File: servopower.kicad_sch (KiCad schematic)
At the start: 53 parts, among them IC1 SIC437DED-T1-GE3, U10 MP28167GQ-A-Z, U9 SC4215

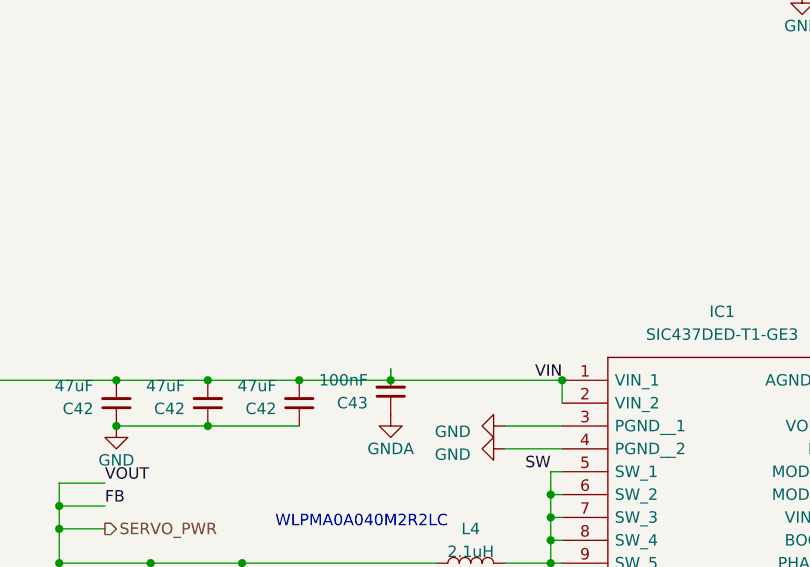
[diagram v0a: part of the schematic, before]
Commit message: latest channges
dont understand why making more copper is good for thermal
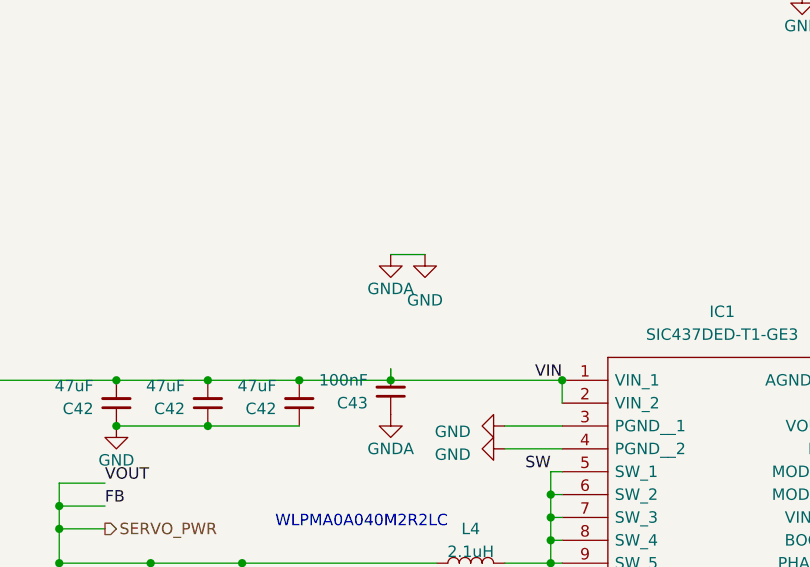
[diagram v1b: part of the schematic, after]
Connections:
- net GNDA is gone; now on net GND: C43.1, C44.2, IC1.16 (AGND_1), IC1.25 (AGND_2), R19.2, R22.2
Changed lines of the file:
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@@
+    (stroke (width 0) (type default))
+  )
+  (wire (pts (xy 186.69 97.79) (xy 190.5 97.79))
     (stroke (width 0) (type default))
   )
@@
     )
   )
+  (symbol (lib_name "GNDA_1") (lib_id "power:GNDA") (at 186.69 97.79 0) (unit 1)
+    (in_bom yes) (on_board yes) (dnp no) (fields_autoplaced)
+    (property "Reference" "#PWR0103" (at 186.69 104.14 0)
+      (effects (font (size 1.27 1.27)) hide)
+    )
+    (property "Value" "GNDA" (at 186.69 101.6 0)
+      (effects (font (size 1.27 1.27)))
+    )
+    (property "Footprint" "" (at 186.69 97.79 0)
+      (effects (font (size 1.27 1.27)) hide)
+    )
+    (property "Datasheet" "" (at 186.69 97.79 0)
+      (effects (font (size 1.27 1.27)) hide)
+    )
+    (pin "1")
+    (instances
+      (project "Canardboard"
+        (path "/7db990e4-92e1-4f99-b4d2-435bbec1ba83/9ac1c7a8-1287-4655-8906-f7f2eef1324f"
+          (reference "#PWR0103") (unit 1)
+        )
+      )
+    )
+  )
   (symbol (lib_name "GND_3") (lib_id "power:GND") (at 62.23 36.83 0) (unit 1)
     (in_bom yes) (on_board yes) (dnp no) (fields_autoplaced)
@@
         )
       )
+    )
+  )
+  (symbol (lib_id "power:GND") (at 190.5 97.79 0) (unit 1)
+    (in_bom yes) (on_board yes) (dnp no)
+    (property "Reference" "#PWR077" (at 190.5 104.14 0)
+      (effects (font (size 1.27 1.27)) hide)
+    )
+    (property "Value" "GND" (at 190.5 102.87 0)
+      (effects (font (size 1.27 1.27)))
+    )
+    (property "Footprint" "" (at 190.5 97.79 0)
+      (effects (font (size 1.27 1.27)) hide)
+    )
+    (property "Datasheet" "" (at 190.5 97.79 0)
+      (effects (font (size 1.27 1.27)) hide)
+    )
+    (pin "1")
+    (instances
+      (project "Canardboard"
+        (path "/7db990e4-92e1-4f99-b4d2-435bbec1ba83/e0402675-af14-46ad-ab53-2a6080ba54c9"
+          (reference "#PWR077") (unit 1)
+        )
+        (path "/7db990e4-92e1-4f99-b4d2-435bbec1ba83/9ac1c7a8-1287-4655-8906-f7f2eef1324f"
+          (reference "#PWR0104") (unit 1)
+        )
+      )
